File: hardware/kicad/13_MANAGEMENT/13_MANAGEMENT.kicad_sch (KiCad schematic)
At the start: 6 parts

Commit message: M3.7: align Slice A passive labels to native pin endpoints
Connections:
- net GND: now also C_MGMT_VREG_AVDD.2, C_MGMT_VREG_IN.2, C_MGMT_VREG_OUT.2
- net MGMT_1V1: now also L_MGMT_CORE.2
- net VREG_AVDD: now also R_MGMT_VREG_AVDD.2
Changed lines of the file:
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@@
   )
   (label "VREG_LX" (at 144.78 80 0) (effects (font (size 1.27 1.27)) (justify right bottom)))
-  (label "MGMT_1V1" (at 155.22 80 180) (effects (font (size 1.27 1.27)) (justify right bottom)))
+  (label "MGMT_1V1" (at 154.94 80 180) (effects (font (size 1.27 1.27)) (justify right bottom)))
   (symbol (lib_id "RetroSBC-management:C_LOCAL") (at 149.86 90 0) (unit 1)
     (exclude_from_sim no) (in_bom yes) (on_board yes)
@@
   )
   (label "MGMT_3V3" (at 144.78 90 0) (effects (font (size 1.27 1.27)) (justify right bottom)))
-  (label "GND" (at 155.22 90 180) (effects (font (size 1.27 1.27)) (justify right bottom)))
+  (label "GND" (at 154.94 90 180) (effects (font (size 1.27 1.27)) (justify right bottom)))
   (symbol (lib_id "RetroSBC-management:C_LOCAL") (at 149.86 100 0) (unit 1)
     (exclude_from_sim no) (in_bom yes) (on_board yes)
@@
   )
   (label "MGMT_1V1" (at 144.78 100 0) (effects (font (size 1.27 1.27)) (justify right bottom)))
-  (label "GND" (at 155.22 100 180) (effects (font (size 1.27 1.27)) (justify right bottom)))
+  (label "GND" (at 154.94 100 180) (effects (font (size 1.27 1.27)) (justify right bottom)))
   (symbol (lib_id "RetroSBC-management:R_LOCAL") (at 149.86 110 0) (unit 1)
     (exclude_from_sim no) (in_bom yes) (on_board yes)
@@
   )
   (label "MGMT_3V3" (at 144.78 110 0) (effects (font (size 1.27 1.27)) (justify right bottom)))
-  (label "VREG_AVDD" (at 155.22 110 180) (effects (font (size 1.27 1.27)) (justify right bottom)))
+  (label "VREG_AVDD" (at 154.94 110 180) (effects (font (size 1.27 1.27)) (justify right bottom)))
   (symbol (lib_id "RetroSBC-management:C_LOCAL") (at 149.86 120 0) (unit 1)
     (exclude_from_sim no) (in_bom yes) (on_board yes)
@@
   )
   (label "VREG_AVDD" (at 144.78 120 0) (effects (font (size 1.27 1.27)) (justify right bottom)))
-  (label "GND" (at 155.22 120 180) (effects (font (size 1.27 1.27)) (justify right bottom)))
+  (label "GND" (at 154.94 120 180) (effects (font (size 1.27 1.27)) (justify right bottom)))
   (label "MGMT_3V3" (at 69.52000000000001 113.97 0)
     (effects (font (size 1.27 1.27)) (justify left bottom))

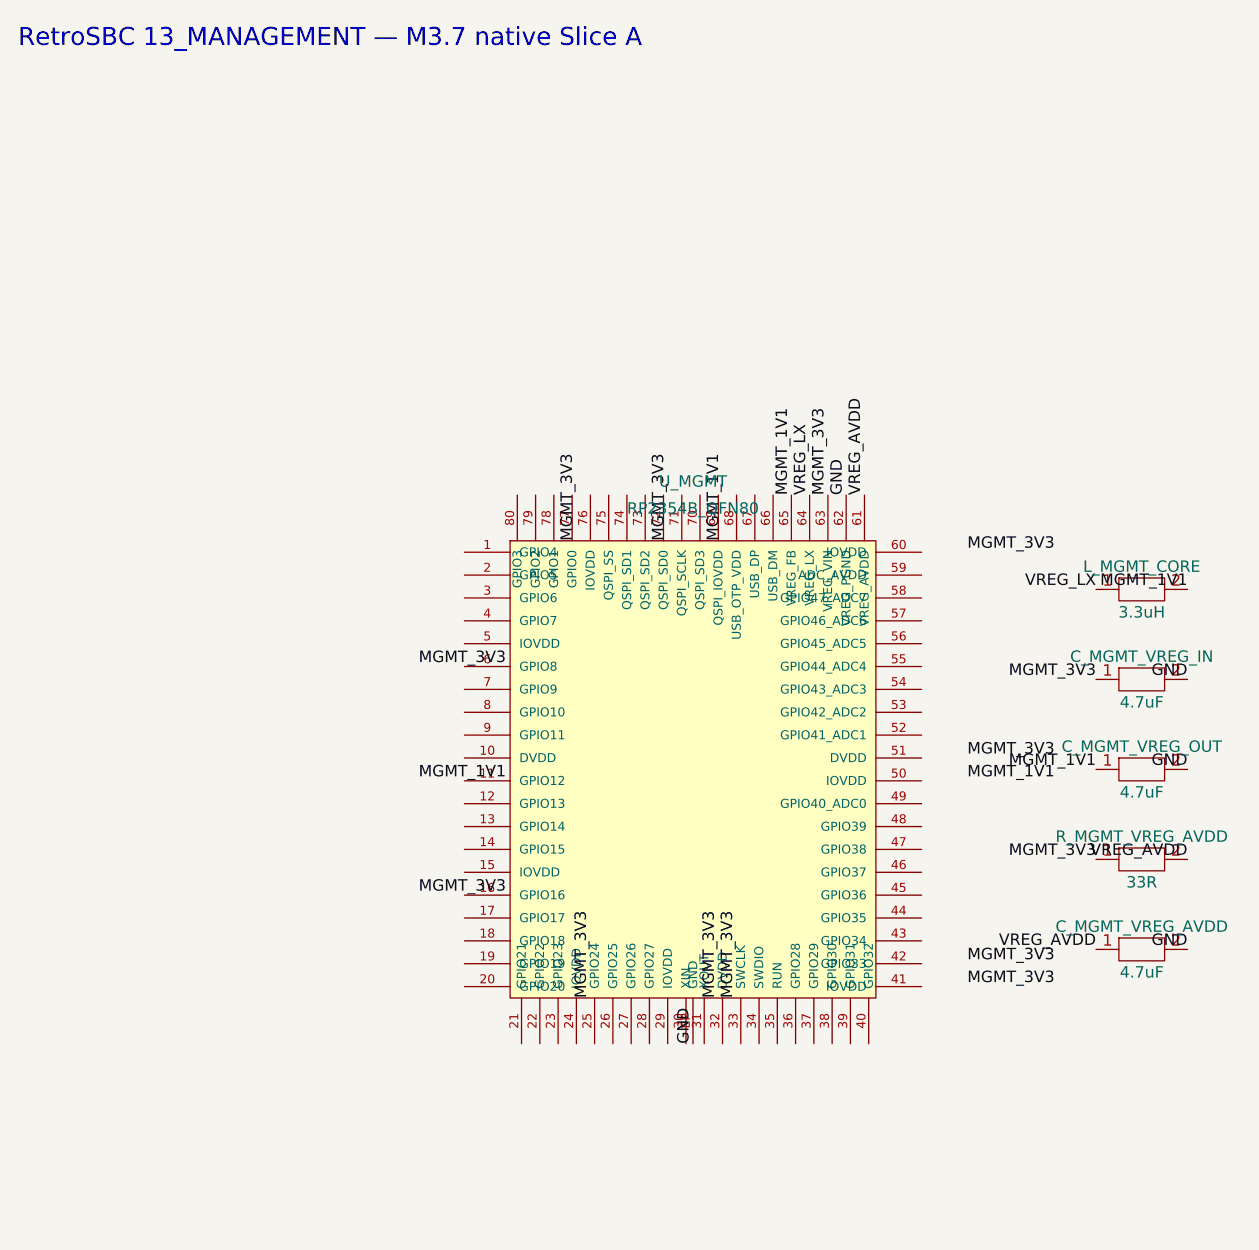
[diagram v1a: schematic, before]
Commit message: M3.7: bind Slice B power labels to ERC-confirmed pin endpoints
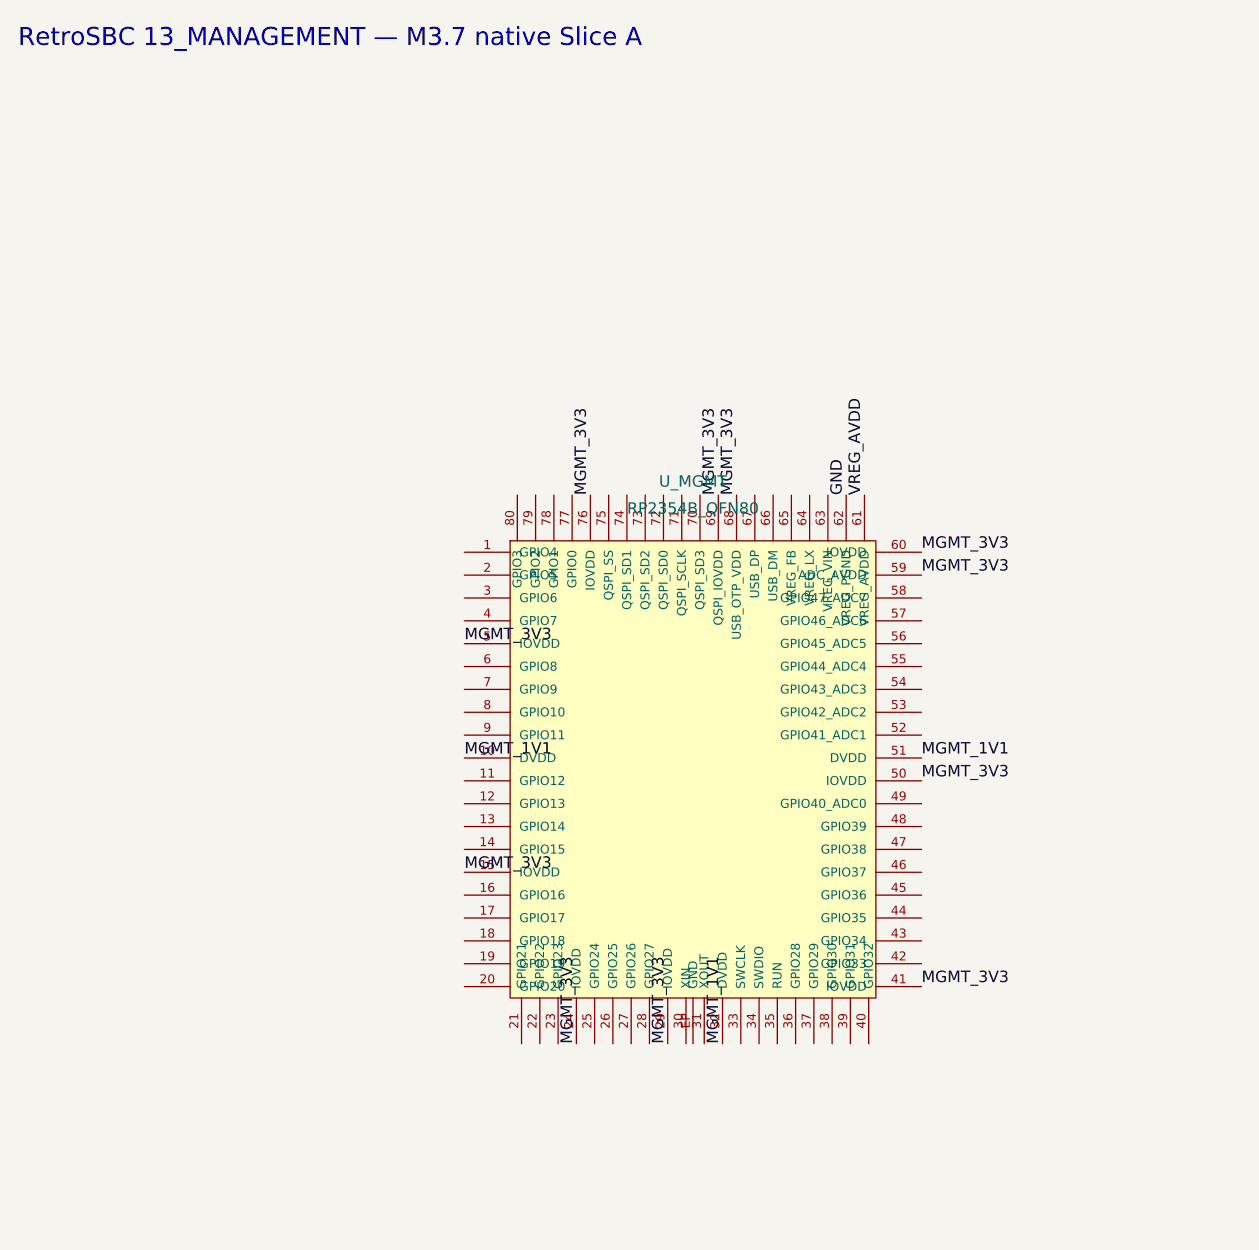
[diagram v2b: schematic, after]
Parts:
- removed C_MGMT_VREG_AVDD, C_MGMT_VREG_IN, C_MGMT_VREG_OUT: 4.7uF, symbol RetroSBC-management:C_LOCAL
- removed L_MGMT_CORE: 3.3uH, symbol RetroSBC-management:L_LOCAL
- removed R_MGMT_VREG_AVDD: 33R, symbol RetroSBC-management:R_LOCAL
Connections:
- net GND: no longer U_MGMT.EP (GND)
- net MGMT_1V1: now also U_MGMT.10 (DVDD), U_MGMT.32 (DVDD), U_MGMT.51 (DVDD); no longer U_MGMT.65 (VREG_FB)
- net MGMT_3V3: now also U_MGMT.15 (IOVDD), U_MGMT.24 (IOVDD), U_MGMT.29 (IOVDD), U_MGMT.41 (IOVDD), U_MGMT.5 (IOVDD), U_MGMT.50 (IOVDD), U_MGMT.59 (ADC_AVDD), U_MGMT.60 (IOVDD), U_MGMT.68 (USB_OTP_VDD), U_MGMT.69 (QSPI_IOVDD), U_MGMT.76 (IOVDD); no longer U_MGMT.63 (VREG_VIN)
- net VREG_LX: no longer names the net of U_MGMT.64 (VREG_LX)
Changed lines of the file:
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@@
   (label "GND" (at 117.02 69.52 90)
     (effects (font (size 1.27 1.27)) (justify left bottom))
-)
-  (label "MGMT_3V3" (at 114.99 69.52 90)
+)  (label "MGMT_3V3" (at 74.6 86.03 180)
     (effects (font (size 1.27 1.27)) (justify left bottom))
 )
-  (label "VREG_LX" (at 112.96 69.52 90)
+  (label "MGMT_1V1" (at 74.6 98.73 180)
     (effects (font (size 1.27 1.27)) (justify left bottom))
 )
-  (label "MGMT_1V1" (at 110.93 69.52 90)
+  (label "MGMT_3V3" (at 74.6 111.43 180)
     (effects (font (size 1.27 1.27)) (justify left bottom))
 )
-  (label "GND" (at 100 130.48 90)
+  (label "MGMT_3V3" (at 87.04 130.48 90)
     (effects (font (size 1.27 1.27)) (justify left bottom))
 )
-  (symbol (lib_id "RetroSBC-management:L_LOCAL") (at 149.86 80 0) (unit 1)
-    (exclude_from_sim no) (in_bom yes) (on_board yes)
-    (property "Reference" "L_MGMT_CORE" (at 149.86 77.46 0) (effects (font (size 1.27 1.27))))
-    (property "Value" "3.3uH" (at 149.86 82.54 0) (effects (font (size 1.27 1.27))))
-    (property "Footprint" "" (at 149.86 80 0) (effects (font (size 1.27 1.27)) hide))
-    (property "Datasheet" "" (at 149.86 80 0) (effects (font (size 1.27 1.27)) hide))
-    (property "Description" "RetroSBC local passive" (at 149.86 80 0) (effects (font (size 1.27 1.27)) hide))
-    (pin "1")
-    (pin "2")
-    (instances (project "RetroSBC-13-MANAGEMENT" (path "/7a5d3d51-9e2f-4d31-b7cb-9fbd10b8c301/21111111-1111-4111-8111-222222222222" (reference "L_MGMT_CORE") (unit 1))))
-  )
-  (label "VREG_LX" (at 144.78 80 0) (effects (font (size 1.27 1.27)) (justify right bottom)))
-  (label "MGMT_1V1" (at 154.94 80 180) (effects (font (size 1.27 1.27)) (justify right bottom)))
-  (symbol (lib_id "RetroSBC-management:C_LOCAL") (at 149.86 90 0) (unit 1)
-    (exclude_from_sim no) (in_bom yes) (on_board yes)
-    (property "Reference" "C_MGMT_VREG_IN" (at 149.86 87.46 0) (effects (font (size 1.27 1.27))))
-    (property "Value" "4.7uF" (at 149.86 92.54 0) (effects (font (size 1.27 1.27))))
-    (property "Footprint" "" (at 149.86 90 0) (effects (font (size 1.27 1.27)) hide))
-    (property "Datasheet" "" (at 149.86 90 0) (effects (font (size 1.27 1.27)) hide))
-    (property "Description" "RetroSBC local passive" (at 149.86 90 0) (effects (font (size 1.27 1.27)) hide))
-    (pin "1")
-    (pin "2")
-    (instances (project "RetroSBC-13-MANAGEMENT" (path "/7a5d3d51-9e2f-4d31-b7cb-9fbd10b8c301/31111111-1111-4111-8111-333333333333" (reference "C_MGMT_VREG_IN") (unit 1))))
-  )
-  (label "MGMT_3V3" (at 144.78 90 0) (effects (font (size 1.27 1.27)) (justify right bottom)))
-  (label "GND" (at 154.94 90 180) (effects (font (size 1.27 1.27)) (justify right bottom)))
-  (symbol (lib_id "RetroSBC-management:C_LOCAL") (at 149.86 100 0) (unit 1)
-    (exclude_from_sim no) (in_bom yes) (on_board yes)
-    (property "Reference" "C_MGMT_VREG_OUT" (at 149.86 97.46 0) (effects (font (size 1.27 1.27))))
-    (property "Value" "4.7uF" (at 149.86 102.54 0) (effects (font (size 1.27 1.27))))
-    (property "Footprint" "" (at 149.86 100 0) (effects (font (size 1.27 1.27)) hide))
-    (property "Datasheet" "" (at 149.86 100 0) (effects (font (size 1.27 1.27)) hide))
-    (property "Description" "RetroSBC local passive" (at 149.86 100 0) (effects (font (size 1.27 1.27)) hide))
-    (pin "1")
-    (pin "2")
-    (instances (project "RetroSBC-13-MANAGEMENT" (path "/7a5d3d51-9e2f-4d31-b7cb-9fbd10b8c301/41111111-1111-4111-8111-444444444444" (reference "C_MGMT_VREG_OUT") (unit 1))))
-  )
-  (label "MGMT_1V1" (at 144.78 100 0) (effects (font (size 1.27 1.27)) (justify right bottom)))
-  (label "GND" (at 154.94 100 180) (effects (font (size 1.27 1.27)) (justify right bottom)))
-  (symbol (lib_id "RetroSBC-management:R_LOCAL") (at 149.86 110 0) (unit 1)
-    (exclude_from_sim no) (in_bom yes) (on_board yes)
-    (property "Reference" "R_MGMT_VREG_AVDD" (at 149.86 107.46 0) (effects (font (size 1.27 1.27))))
-    (property "Value" "33R" (at 149.86 112.54 0) (effects (font (size 1.27 1.27))))
-    (property "Footprint" "" (at 149.86 110 0) (effects (font (size 1.27 1.27)) hide))
-    (property "Datasheet" "" (at 149.86 110 0) (effects (font (size 1.27 1.27)) hide))
-    (property "Description" "RetroSBC local passive" (at 149.86 110 0) (effects (font (size 1.27 1.27)) hide))
-    (pin "1")
-    (pin "2")
-    (instances (project "RetroSBC-13-MANAGEMENT" (path "/7a5d3d51-9e2f-4d31-b7cb-9fbd10b8c301/51111111-1111-4111-8111-555555555555" (reference "R_MGMT_VREG_AVDD") (unit 1))))
-  )
-  (label "MGMT_3V3" (at 144.78 110 0) (effects (font (size 1.27 1.27)) (justify right bottom)))
-  (label "VREG_AVDD" (at 154.94 110 180) (effects (font (size 1.27 1.27)) (justify right bottom)))
-  (symbol (lib_id "RetroSBC-management:C_LOCAL") (at 149.86 120 0) (unit 1)
-    (exclude_from_sim no) (in_bom yes) (on_board yes)
-    (property "Reference" "C_MGMT_VREG_AVDD" (at 149.86 117.46 0) (effects (font (size 1.27 1.27))))
-    (property "Value" "4.7uF" (at 149.86 122.54 0) (effects (font (size 1.27 1.27))))
-    (property "Footprint" "" (at 149.86 120 0) (effects (font (size 1.27 1.27)) hide))
-    (property "Datasheet" "" (at 149.86 120 0) (effects (font (size 1.27 1.27)) hide))
-    (property "Description" "RetroSBC local passive" (at 149.86 120 0) (effects (font (size 1.27 1.27)) hide))
-    (pin "1")
-    (pin "2")
-    (instances (project "RetroSBC-13-MANAGEMENT" (path "/7a5d3d51-9e2f-4d31-b7cb-9fbd10b8c301/61111111-1111-4111-8111-666666666666" (reference "C_MGMT_VREG_AVDD") (unit 1))))
-  )
-  (label "VREG_AVDD" (at 144.78 120 0) (effects (font (size 1.27 1.27)) (justify right bottom)))
-  (label "GND" (at 154.94 120 180) (effects (font (size 1.27 1.27)) (justify right bottom)))
-  (label "MGMT_3V3" (at 69.52000000000001 113.97 0)
+  (label "MGMT_3V3" (at 97.19 130.48 90)
     (effects (font (size 1.27 1.27)) (justify left bottom))
 )
-  (label "MGMT_1V1" (at 69.52000000000001 101.27 0)
+  (label "MGMT_1V1" (at 103.28 130.48 90)
     (effects (font (size 1.27 1.27)) (justify left bottom))
 )
-  (label "MGMT_3V3" (at 69.52000000000001 88.57 0)
+  (label "MGMT_3V3" (at 125.4 124.13 0)
     (effects (font (size 1.27 1.27)) (justify left bottom))
 )
-  (label "MGMT_3V3" (at 87.03999999999999 74.6 90)
+  (label "MGMT_3V3" (at 125.4 101.27 0)
     (effects (font (size 1.27 1.27)) (justify left bottom))
 )
-  (label "MGMT_3V3" (at 97.19 74.6 90)
+  (label "MGMT_1V1" (at 125.4 98.73 0)
     (effects (font (size 1.27 1.27)) (justify left bottom))
 )
-  (label "MGMT_1V1" (at 103.28 74.6 90)
+  (label "MGMT_3V3" (at 125.4 78.41 0)
     (effects (font (size 1.27 1.27)) (justify left bottom))
 )
-  (label "MGMT_3V3" (at 130.48 75.87 180)
+  (label "MGMT_3V3" (at 125.4 75.87 0)
     (effects (font (size 1.27 1.27)) (justify left bottom))
 )
-  (label "MGMT_3V3" (at 130.48 98.73 180)
+  (label "MGMT_3V3" (at 104.84 69.52 270)
     (effects (font (size 1.27 1.27)) (justify left bottom))
 )
-  (label "MGMT_1V1" (at 130.48 101.27 180)
+  (label "MGMT_3V3" (at 102.81 69.52 270)
     (effects (font (size 1.27 1.27)) (justify left bottom))
 )
-  (label "MGMT_3V3" (at 130.48 121.59 180)
+  (label "MGMT_3V3" (at 88.6 69.52 270)
     (effects (font (size 1.27 1.27)) (justify left bottom))
 )
-  (label "MGMT_3V3" (at 130.48 124.13 180)
-    (effects (font (size 1.27 1.27)) (justify left bottom))
-)
-  (label "MGMT_3V3" (at 104.84 125.4 270)
-    (effects (font (size 1.27 1.27)) (justify left bottom))
-)
-  (label "MGMT_3V3" (at 102.81 125.4 270)
-    (effects (font (size 1.27 1.27)) (justify left bottom))
-)
-  (label "MGMT_3V3" (at 88.60000000000001 125.4 270)
-    (effects (font (size 1.27 1.27)) (justify left bottom))
-)
